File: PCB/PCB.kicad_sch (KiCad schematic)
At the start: 2 parts

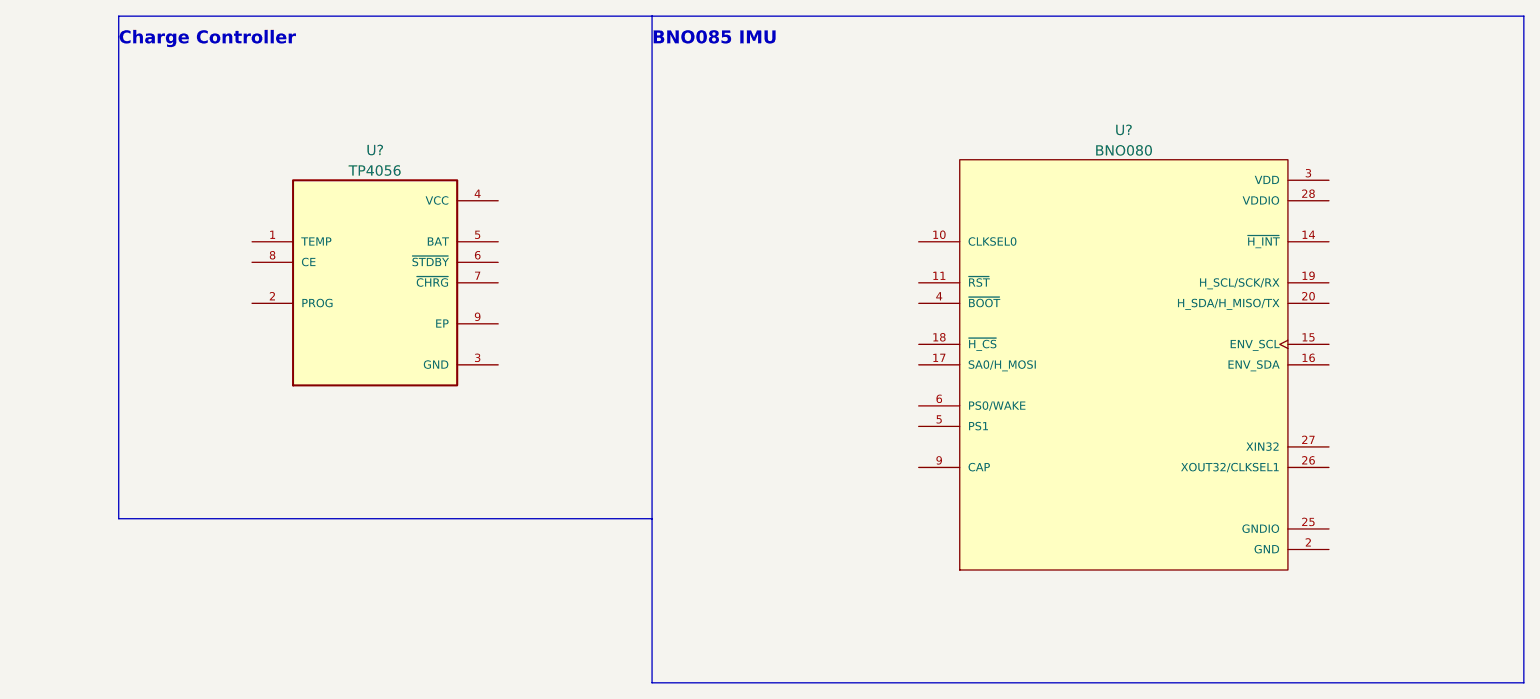
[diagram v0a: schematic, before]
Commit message: bno085 schematic done
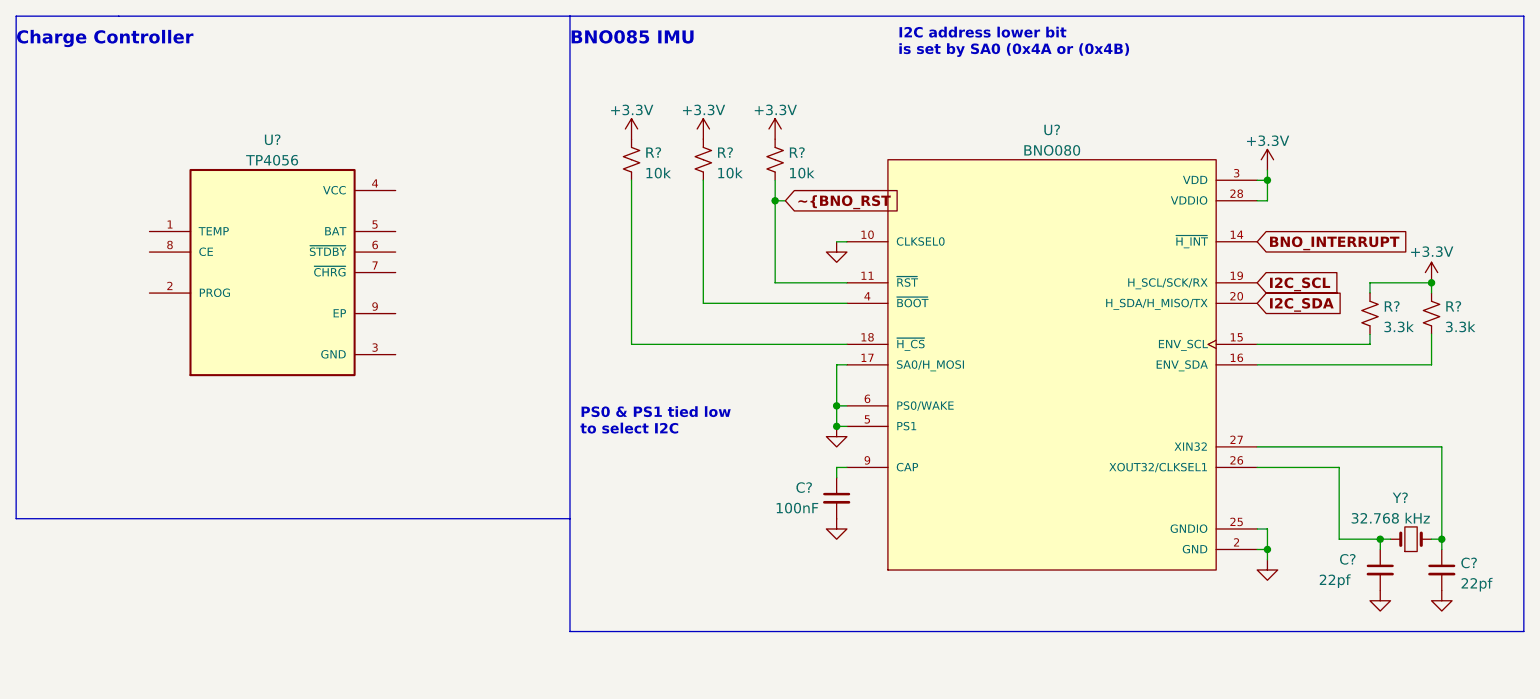
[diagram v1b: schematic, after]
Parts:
- added C?: 100nF, symbol Device:C_Small
- added C? (x2): 22pf, symbol Device:C_Small
- added R? (x3): 10k, symbol Device:R_Small_US
- added R? (x2): 3.3k, symbol Device:R_Small_US
- added Y?: 32.768 kHz, symbol Device:Crystal_Small
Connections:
- net GND: now reaches U?.10 (CLKSEL0)
- net GND: now also U?.17 (SA0/H_MOSI), U?.2 (GND), U?.25 (GNDIO), U?.5 (PS1), U?.6 (PS0/WAKE), C?.2, C?.2, C?.2
- net ~{BNO_RST: now reaches U?.11 (~{RST})
- net ~{BNO_RST: now also R?.2
- net BNO_INTERRUPT: now reaches U?.14 (~{H_INT})
- net at U?.15 (ENV_SCL): now also R?.2
- net at U?.16 (ENV_SDA): now also R?.2
- net at U?.18 (~{H_CS}): now also R?.2
- net I2C_SCL: now reaches U?.19 (H_SCL/SCK/RX)
- net I2C_SDA: now reaches U?.20 (H_SDA/H_MISO/TX)
- net at U?.26 (XOUT32/CLKSEL1): now also C?.1, Y?.1
- net at U?.27 (XIN32): now also C?.1, Y?.2
- net +3.3V: now reaches U?.28 (VDDIO)
- net +3.3V: now also U?.3 (VDD), R?.1, R?.1, R?.1, R?.1, R?.1
- net at U?.4 (~{BOOT}): now also R?.2
- net at U?.9 (CAP): now also C?.1
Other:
- note added: "I2C address lower bit is set by SA0 (0x4A or (0x4B)"
- note added: "PS0 & PS1 tied low to select I2C"
- moved on the sheet: U?

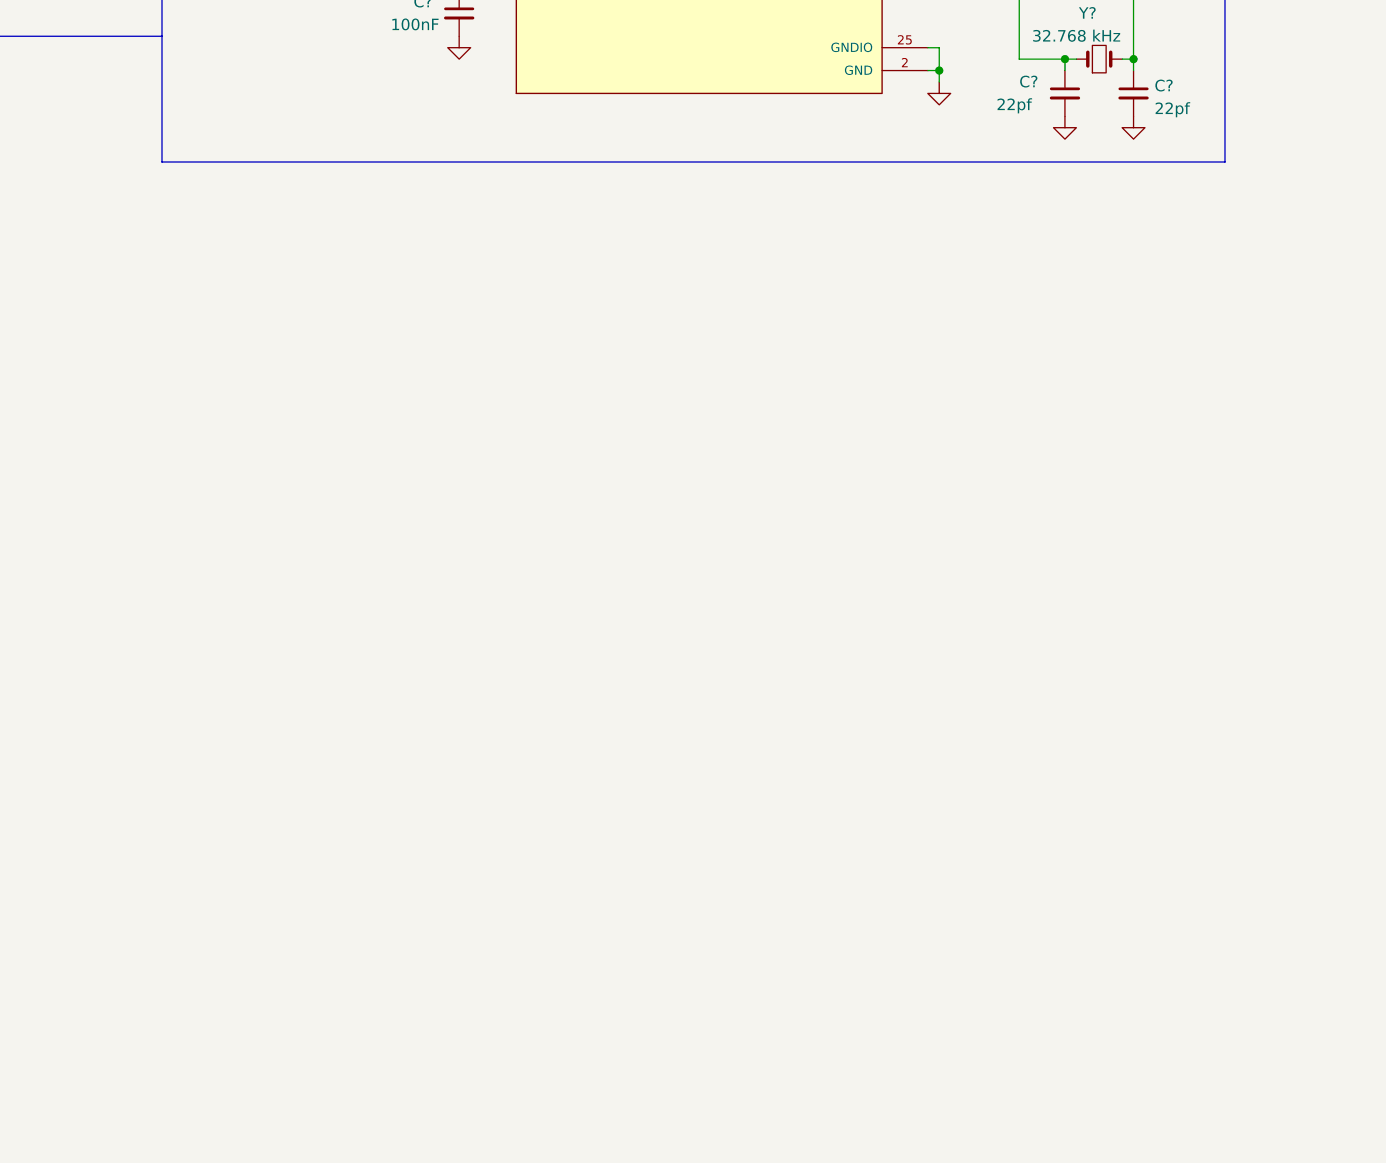
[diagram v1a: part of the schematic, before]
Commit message: buck-boost schematic added
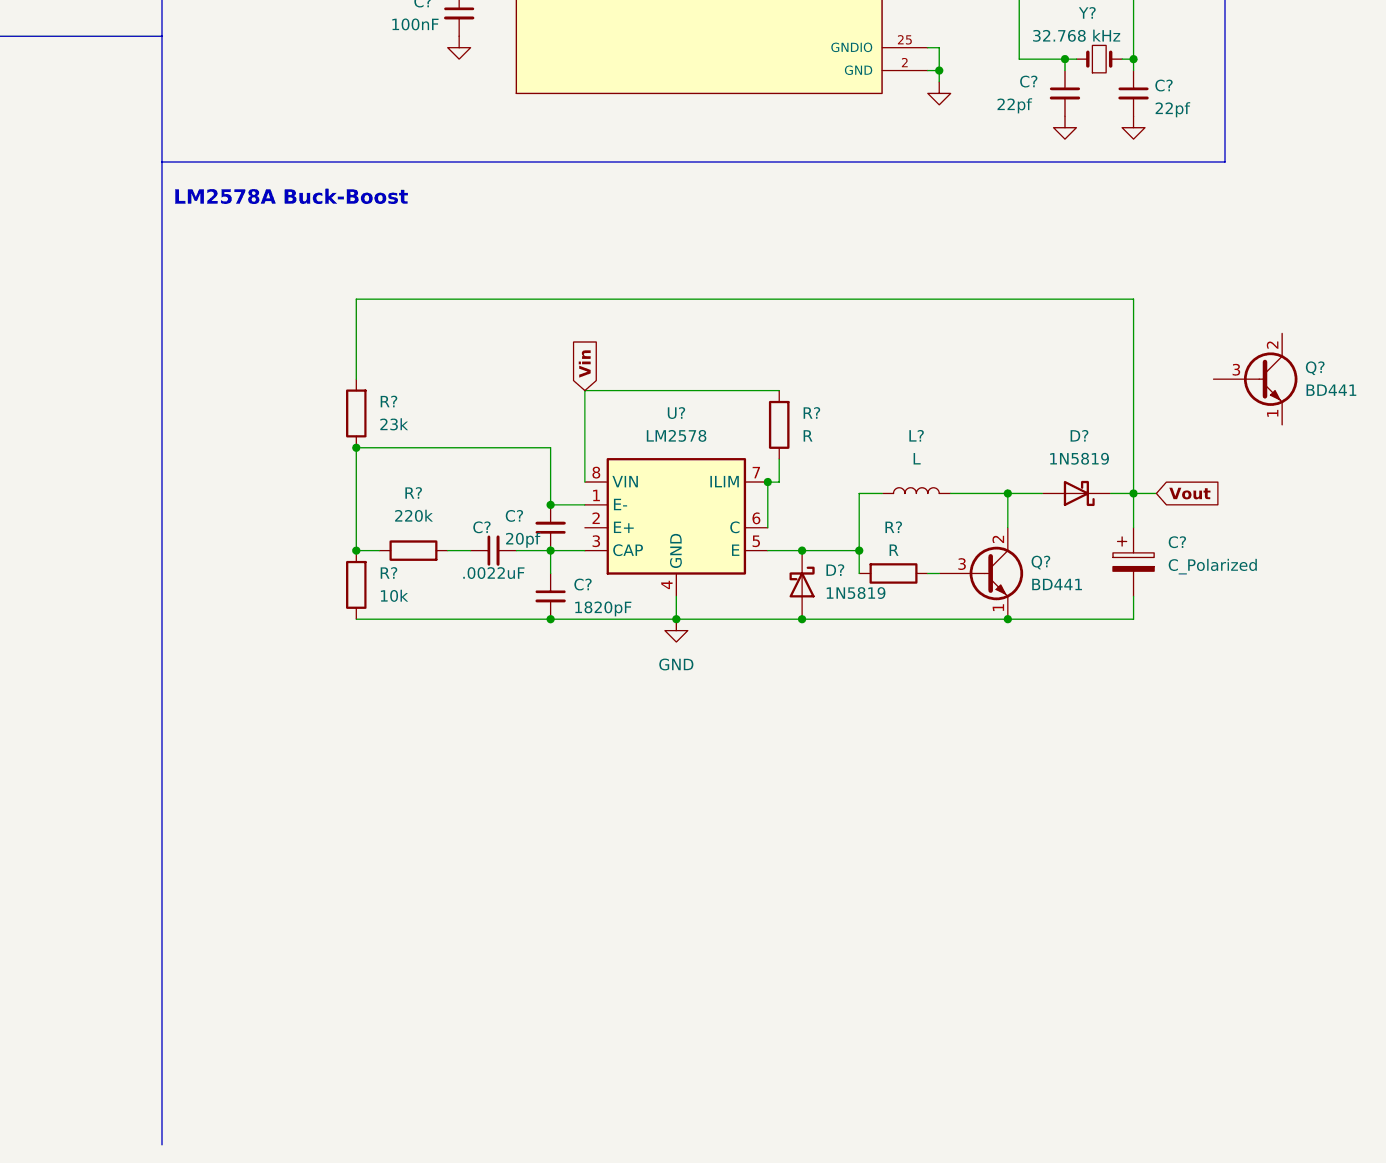
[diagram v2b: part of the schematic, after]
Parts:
- added C?: C_Polarized, symbol Device:C_Polarized
- added C?: 20pf, symbol Device:C_Small
- added C?: .0022uF, symbol Device:C_Small
- added C?: 1820pF, symbol Device:C_Small
- added D? (x2): 1N5819, Diode_THT:D_DO-41_SOD81_P10.16mm_Horizontal, symbol Diode:1N5819
- added L?: L, symbol Device:L
- added Q? (x2): BD441, Package_TO_SOT_THT:TO-126-3_Vertical, symbol Transistor_BJT:BD441
- added R?: 220k, symbol Device:R
- added R? (x2): R, symbol Device:R
- added R?: 23k, symbol Device:R
- added R?: 10k, symbol Device:R
- added U?: LM2578, symbol Regulator_Switching:LM2578
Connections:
- net GND: now also C?.2, C?.2, D?.2 (A), Q?.1 (E), R?.1, U?.4 (GND)
- new net: C?.2, R?.1, R?.1, R?.2, U?.1 (E-)
- new net: C?.1, C?.1, C?.2, U?.3 (CAP)
- new net: D?.1 (K), L?.1, R?.2, U?.5 (E)
- new net: R?.1, U?.6 (C), U?.7 (ILIM)
- new net: C?.1, R?.2
- new net: D?.2 (A), L?.2, Q?.2 (C)
- new net: Q?.3 (B), R?.1
- new net Vin: R?.2, U?.8 (VIN)
- new net Vout: C?.1, D?.1 (K), R?.2
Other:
- note added: "LM2578A Buck-Boost"

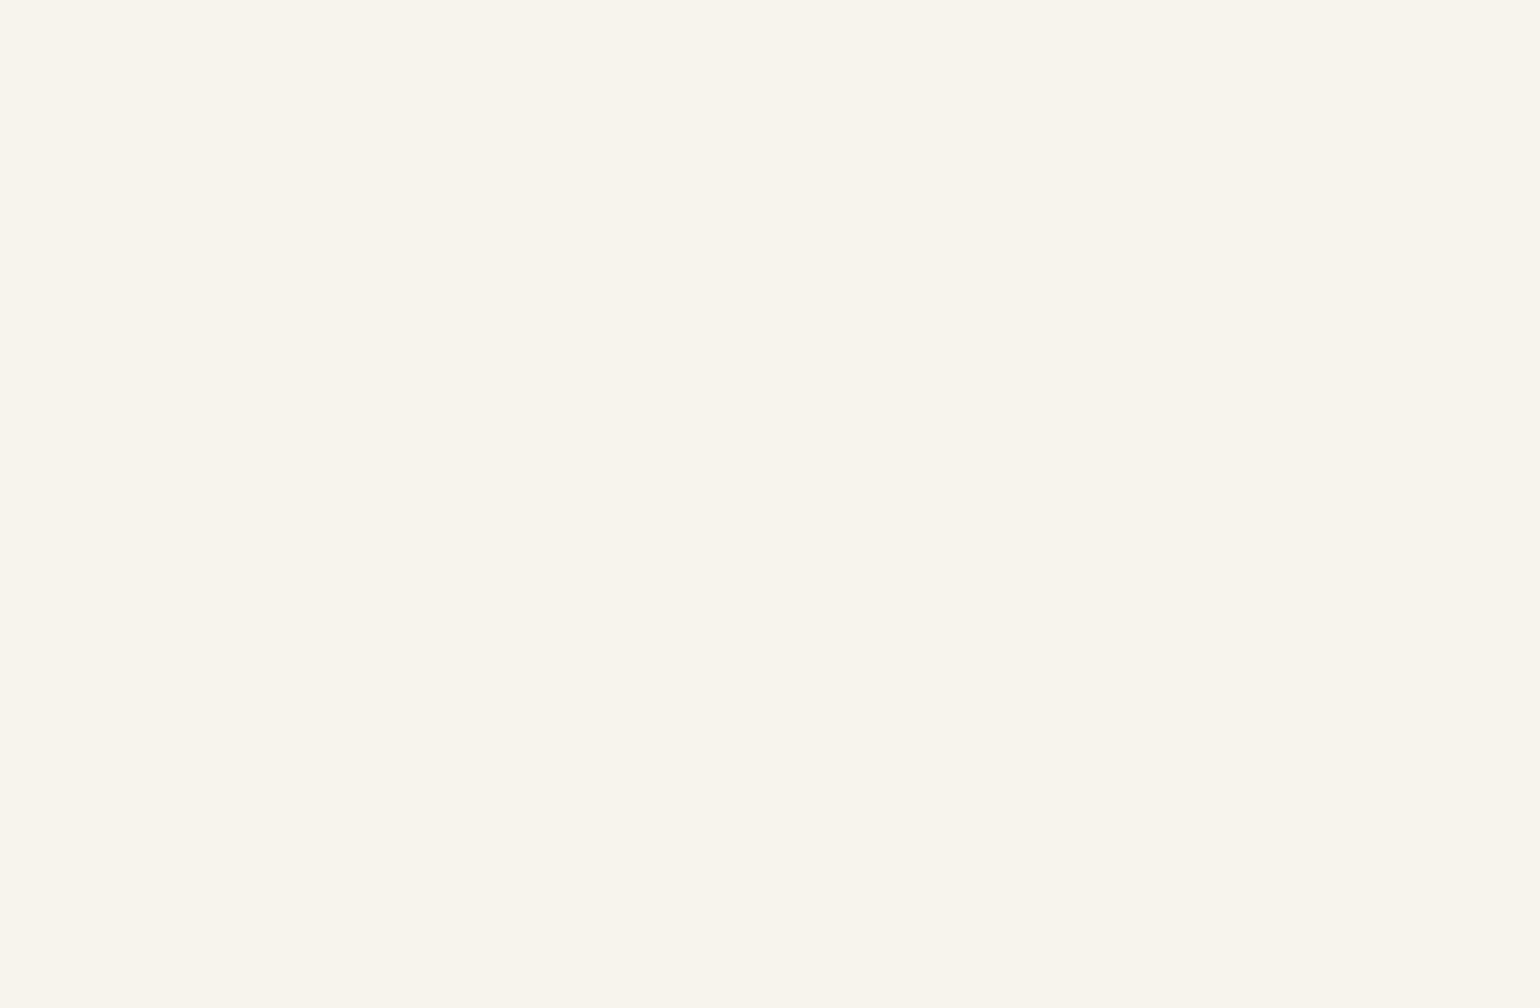
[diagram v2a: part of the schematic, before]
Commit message: added micro and voltage input schematics
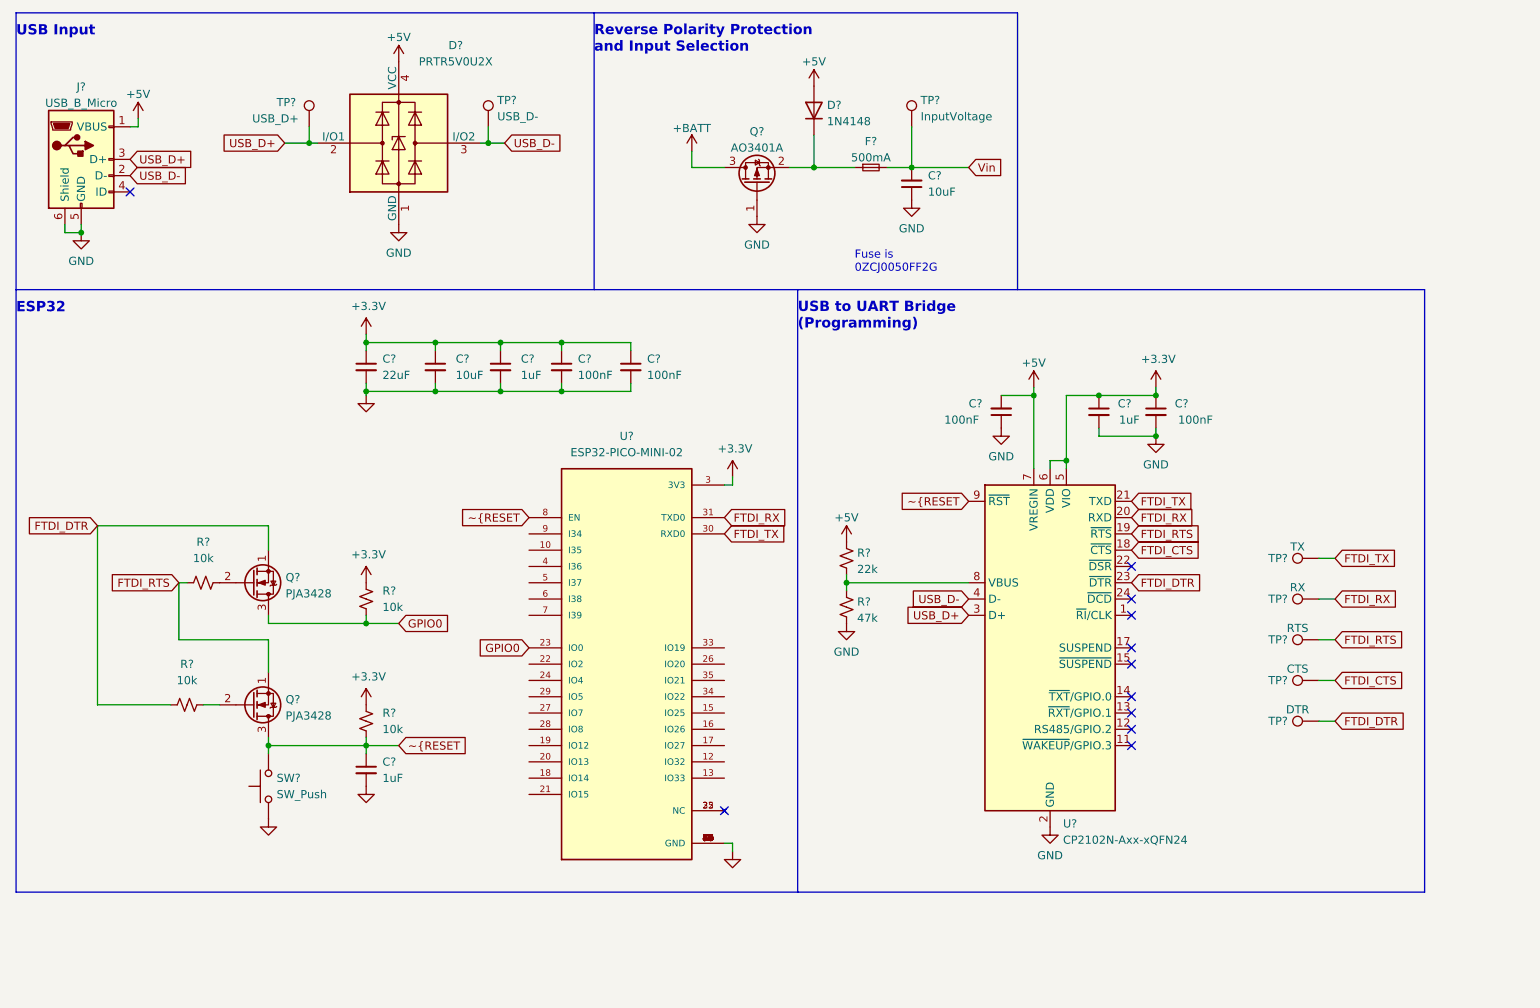
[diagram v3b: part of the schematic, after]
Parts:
- added C? (x3): 1uF, symbol Device:C_Small
- added C?: 22uF, symbol Device:C_Small
- added C? (x2): 10uF, symbol Device:C_Small
- added C? (x4): 100nF, symbol Device:C_Small
- added D?: 1N4148, Diode_THT:D_DO-35_SOD27_P7.62mm_Horizontal, symbol Diode:1N4148
- added D?: PRTR5V0U2X, Package_TO_SOT_SMD:SOT-143, symbol Power_Protection:PRTR5V0U2X
- added F?: 500mA, symbol Device:Fuse_Small
- added J?: USB_B_Micro, symbol Connector:USB_B_Micro
- added Q?: AO3401A, Package_TO_SOT_SMD:SOT-23, symbol Transistor_FET:AO3401A
- added Q? (x2): PJA3428, Package_TO_SOT_THT:TO-92_Inline, symbol Transistor_FET:2N7000
- added R? (x4): 10k, symbol Device:R_Small_US
- added R?: 47k, symbol Device:R_Small_US
- added R?: 22k, symbol Device:R_Small_US
- added SW?: SW_Push, symbol Switch:SW_Push
- added TP?: USB_D+, symbol Connector:TestPoint
- added TP?: CTS, symbol Connector:TestPoint
- added TP?: RTS, symbol Connector:TestPoint
- added TP?: RX, symbol Connector:TestPoint
- added TP?: USB_D-, symbol Connector:TestPoint
- added TP?: InputVoltage, symbol Connector:TestPoint
- added TP?: DTR, symbol Connector:TestPoint
- added TP?: TX, symbol Connector:TestPoint
- added U?: CP2102N-Axx-xQFN24, Package_DFN_QFN:QFN-24-1EP_4x4mm_P0.5mm_EP2.6x2.6mm, symbol Interface_USB:CP2102N-Axx-xQFN24
- added U?: ESP32-PICO-MINI-02, MODULE_ESP32-PICO-MINI-02, symbol ESP32-PICO-MINI-02:ESP32-PICO-MINI-02
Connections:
- net GND: now also C?.1, C?.1, C?.2, C?.2, C?.2, C?.2, C?.2, C?.2, C?.2, C?.2, D?.1 (GND), J?.5 (GND), J?.6 (Shield), Q?.1 (G), R?.2, SW?.1, U?.1 (GND), U?.11 (GND), U?.14 (GND), U?.2 (GND), U?.2 (GND), U?.25 (GND), U?.36 (GND), U?.37 (GND), U?.38 (GND), U?.39 (GND), U?.40 (GND), U?.41 (GND), U?.42 (GND), U?.43 (GND), U?.44 (GND), U?.45 (GND), U?.46 (GND), U?.47 (GND), U?.48 (GND), U?.49 (GND), U?.50 (GND), U?.51 (GND), U?.52 (GND), U?.53 (GND), U?.54 (GND), U?.55 (GND), U?.56 (GND), U?.57 (GND), U?.58 (GND), U?.59 (GND), U?.60 (GND), U?.61 (GND)
- net Vin: now also C?.2, F?.2, TP?.1
- new net: D?.1 (K), F?.1, Q?.2 (S)
- new net: R?.1, R?.2, U?.8 (VBUS)
- new net: Q?.2 (G), R?.2 (x2)
- new net: U?.25 (NC), U?.32 (NC)
- new net +3V3: C?.1, C?.1, C?.1, C?.1, C?.1, C?.1, C?.1, R?.1, R?.1, U?.3 (3V3), U?.5 (VIO), U?.6 (VDD)
- new net +5V: C?.2, D?.2 (A), D?.4 (VCC), J?.1 (VBUS), R?.1, U?.7 (VREGIN)
- new net +BATT: Q?.3 (D)
- new net FTDI_CTS: TP?.1, U?.18 (~{CTS})
- new net FTDI_DTR: Q?.1 (S), R?.1, TP?.1, U?.23 (~{DTR})
- new net FTDI_RTS: Q?.1 (S), R?.1, TP?.1, U?.19 (~{RTS})
- new net FTDI_RX: TP?.1, U?.20 (RXD), U?.31 (TXD0)
- new net FTDI_TX: TP?.1, U?.21 (TXD), U?.30 (RXD0)
- new net GPIO0: Q?.3 (D), R?.2, U?.23 (IO0)
- new net USB_D+: D?.2 (I/O1), J?.3 (D+), TP?.1, U?.3 (D+)
- new net USB_D-: D?.3 (I/O2), J?.2 (D-), TP?.1, U?.4 (D-)
- new net ~{RESET: C?.1, Q?.3 (D), R?.2, SW?.2, U?.8 (EN), U?.9 (~{RST})
- no-connect marks 0 -> 11
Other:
- note added: "ESP32"
- note added: "Fuse is 0ZCJ0050FF2G"
- note added: "Reverse Polarity Protection and Input Selection"
- note added: "USB Input"
- note added: "USB to UART Bridge (Programming)"
